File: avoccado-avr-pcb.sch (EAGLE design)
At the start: 24 parts, among them IC1 MCP1703CB, Q1 #MHz, Q2 MOSFET-NCHANNEL2N7002PW, U1 ATMEGA168#, U2 MCP73831, X1 Micro USB

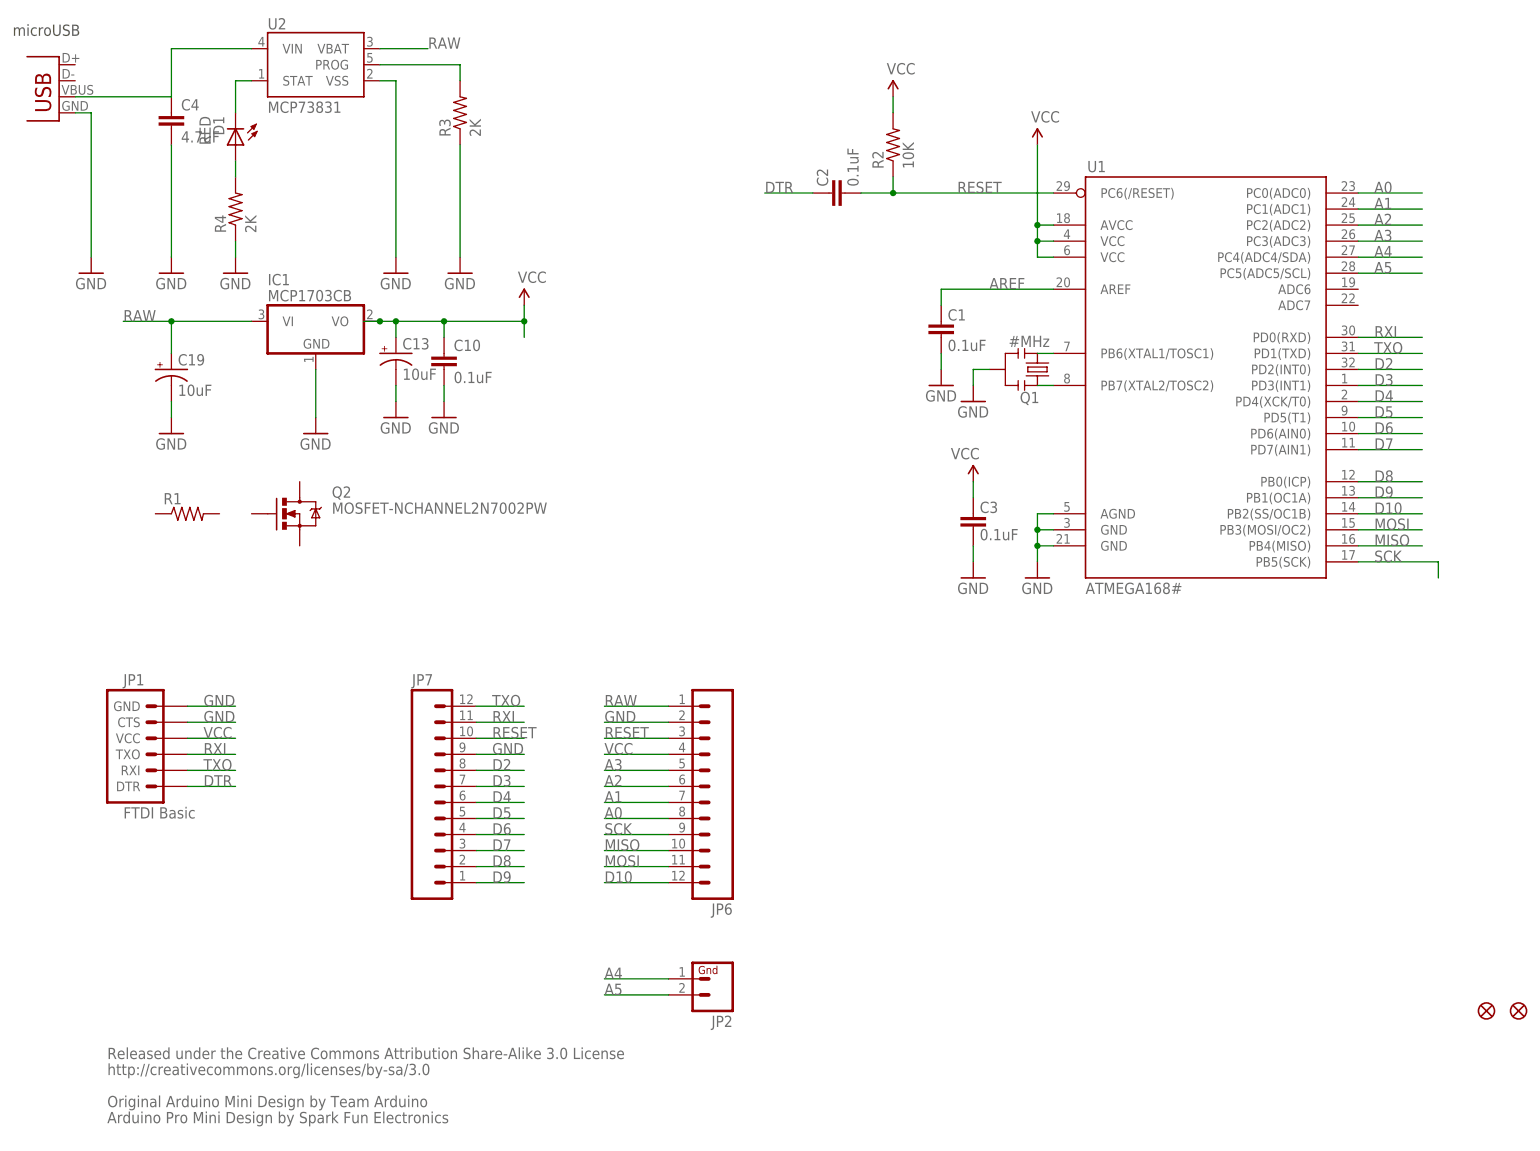
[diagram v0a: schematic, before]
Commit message: add n-chan LL mosfet for vibrator
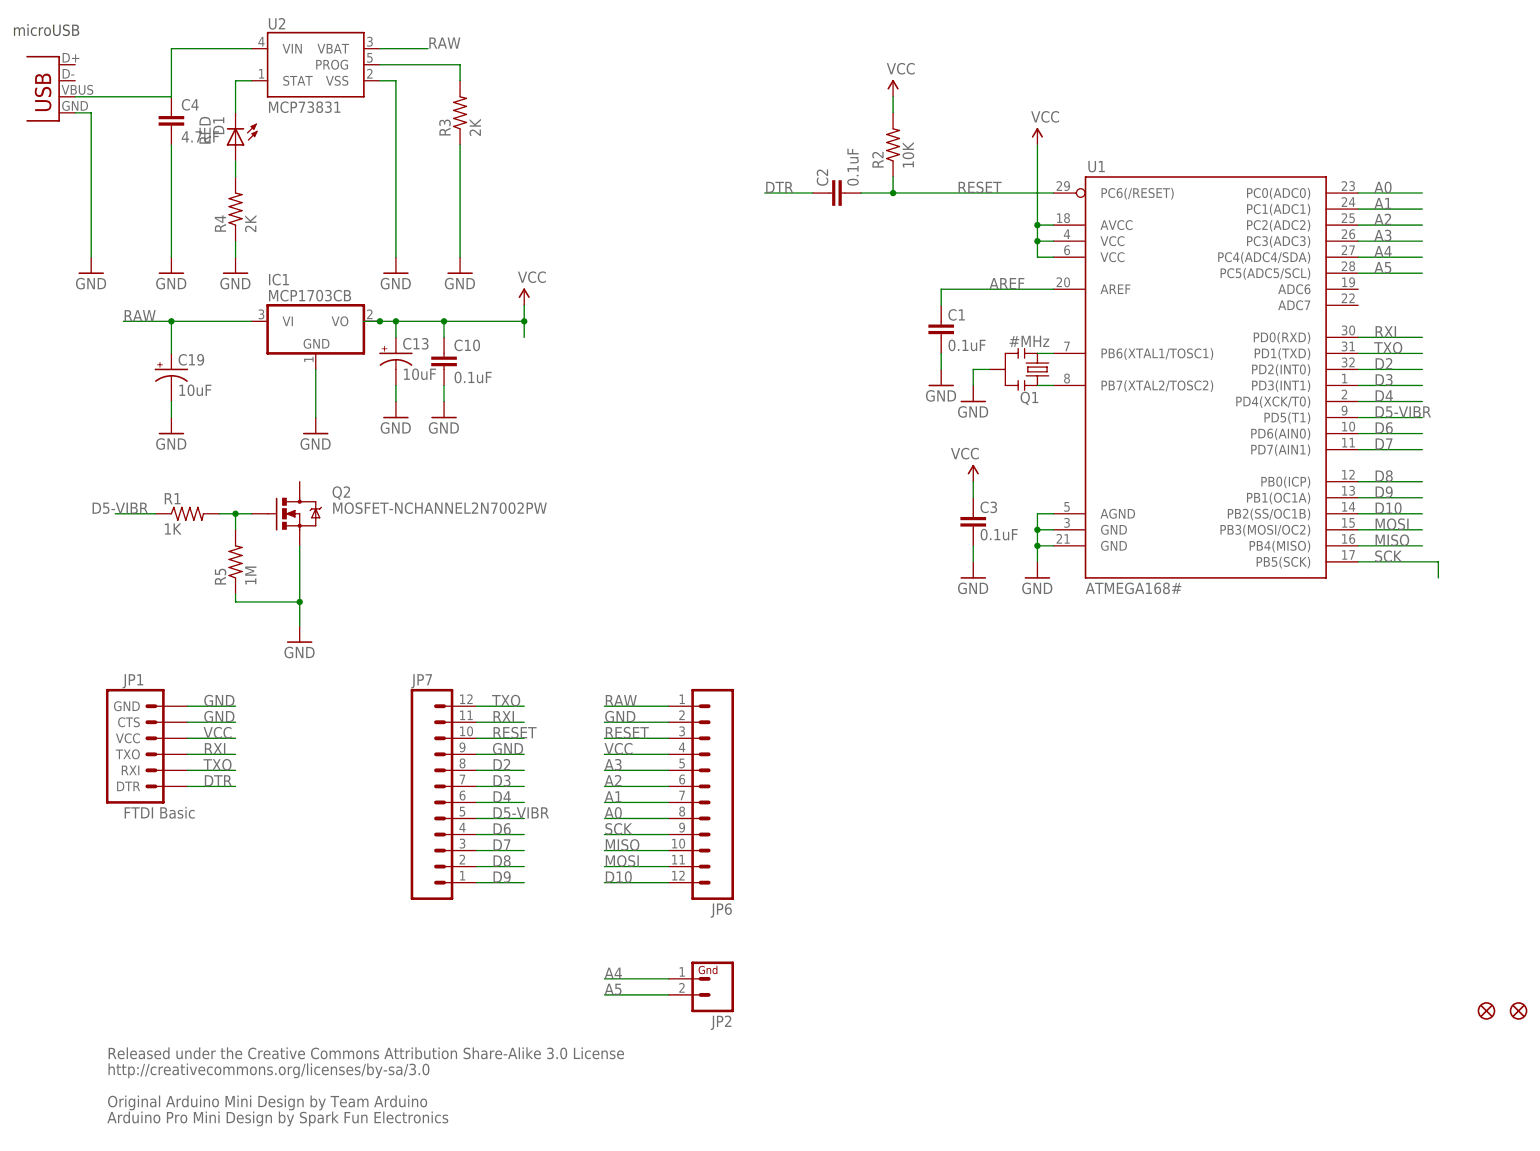
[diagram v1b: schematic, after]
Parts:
- added R5: 1M, SparkFun-Passives:RESISTOR0805-RES
- R1: value (none) -> 1K
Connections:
- removed net D5: JP7.5, U1.PD5(T1)
- new net D5-VIBR: JP7.5, R1.1, U1.PD5(T1)
- new net N$6: Q2.G, R1.2, R5.2
- net GND: now also Q2.S, R5.1
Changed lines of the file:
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@@
 <setting verticaltext="up"/>
 </settings>
-<grid distance="0.1" unitdist="inch" unit="inch" style="lines" multiple="1" display="no" altdistance="0.01" altunitdist="inch" altunit="inch"/>
+<grid distance="0.05" unitdist="inch" unit="inch" style="lines" multiple="1" display="yes" altdistance="0.005" altunitdist="inch" altunit="inch"/>
 <layers>
 <layer number="1" name="Top" color="4" fill="1" visible="no" active="no"/>
@@
 <part name="C2" library="SparkFun" deviceset="CAP" device="0402" value="0.1uF"/>
 <part name="Q2" library="SparkFun-DiscreteSemi" deviceset="MOSFET-NCHANNEL" device="2N7002PW"/>
-<part name="R1" library="SparkFun-Passives" deviceset="RESISTOR" device="0805-RES"/>
+<part name="R1" library="SparkFun-Passives" deviceset="RESISTOR" device="0805-RES" value="1K"/>
 <part name="IC1" library="linear" deviceset="MCP1703" device="CB"/>
 <part name="U2" library="SparkFun" deviceset="MCP73831" device=""/>
@@
 <part name="GND6" library="SparkFun" deviceset="GND" device=""/>
 <part name="GND8" library="SparkFun" deviceset="GND" device=""/>
+<part name="GND9" library="SparkFun" deviceset="GND" device=""/>
+<part name="R5" library="SparkFun-Passives" deviceset="RESISTOR" device="0805-RES" value="1M"/>
 </parts>
 <sheets>
@@
 <instance part="GND6" gate="1" x="38.1" y="142.24"/>
 <instance part="GND8" gate="1" x="27.94" y="142.24"/>
+<instance part="GND9" gate="1" x="48.26" y="83.82"/>
+<instance part="R5" gate="G$1" x="38.1" y="96.52" rot="R90"/>
 </instances>
 <busses>
@@
 <pinref part="GND8" gate="1" pin="GND"/>
 <wire x1="27.94" y1="162.56" x2="27.94" y2="144.78" width="0.1524" layer="91"/>
+</segment>
+<segment>
+<pinref part="GND9" gate="1" pin="GND"/>
+<pinref part="Q2" gate="G$1" pin="S"/>
+<wire x1="48.26" y1="86.36" x2="48.26" y2="90.17" width="0.1524" layer="91"/>
+<wire x1="48.26" y1="90.17" x2="48.26" y2="99.06" width="0.1524" layer="91"/>
+<wire x1="48.26" y1="90.17" x2="38.1" y2="90.17" width="0.1524" layer="91"/>
+<junction x="48.26" y="90.17"/>
+<pinref part="R5" gate="G$1" pin="1"/>
+<wire x1="38.1" y1="90.17" x2="38.1" y2="91.44" width="0.1524" layer="91"/>
 </segment>
 </net>
@@
 </segment>
 </net>
-<net name="D5" class="0">
+<net name="D5-VIBR" class="0">
 <segment>
 <wire x1="76.2" y1="55.88" x2="83.82" y2="55.88" width="0.1524" layer="91"/>
@@
 <label x="218.44" y="119.38" size="1.778" layer="95"/>
 <pinref part="U1" gate="G$1" pin="PD5(T1)"/>
+</segment>
+<segment>
+<pinref part="R1" gate="G$1" pin="1"/>
+<wire x1="25.4" y1="104.14" x2="19.05" y2="104.14" width="0.1524" layer="91"/>
+<label x="15.24" y="104.14" size="1.778" layer="95"/>
 </segment>
 </net>
@@
 </segment>
 </net>
+<net name="N$6" class="0">
+<segment>
+<pinref part="R1" gate="G$1" pin="2"/>
+<pinref part="Q2" gate="G$1" pin="G"/>
+<wire x1="35.56" y1="104.14" x2="38.1" y2="104.14" width="0.1524" layer="91"/>
+<pinref part="R5" gate="G$1" pin="2"/>
+<wire x1="38.1" y1="104.14" x2="40.64" y2="104.14" width="0.1524" layer="91"/>
+<wire x1="38.1" y1="101.6" x2="38.1" y2="104.14" width="0.1524" layer="91"/>
+<junction x="38.1" y="104.14"/>
+</segment>
+</net>

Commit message: m
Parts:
- D1: value RED -> CHARGE LED
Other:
- note added: "Original Arduino Pro Mini Design by Spark Fun Electronics"
- note added: "Released under the Creative Commons Attribution Share-Alike 4.0 License"
- note removed: "Arduino Pro Mini Design by Spark Fun Electronics"
- note removed: "Released under the Creative Commons Attribution Share-Alike 3.0 License"
- note removed: "http://creativecommons.org/licenses/by-sa/3.0"
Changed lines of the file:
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@@
 <part name="R3" library="SparkFun-Resistors" deviceset="RESISTOR" device="0805-RES" value="2K"/>
 <part name="GND3" library="SparkFun" deviceset="GND" device=""/>
-<part name="D1" library="SparkFun" deviceset="LED" device="0603" value="RED"/>
+<part name="D1" library="SparkFun" deviceset="LED" device="0603" value="CHARGE LED"/>
 <part name="GND15" library="SparkFun" deviceset="GND" device=""/>
 <part name="X1" library="SparkFun" deviceset="USB" device="-MICROB" value="Micro USB"/>
@@
 <sheet>
 <plain>
-<text x="17.78" y="17.78" size="1.778" layer="95">Released under the Creative Commons Attribution Share-Alike 3.0 License</text>
-<text x="17.78" y="15.24" size="1.778" layer="95">http://creativecommons.org/licenses/by-sa/3.0</text>
+<text x="17.78" y="17.78" size="1.778" layer="95">Released under the Creative Commons Attribution Share-Alike 4.0 License</text>
 <text x="17.78" y="10.16" size="1.778" layer="95">Original Arduino Mini Design by Team Arduino</text>
-<text x="17.78" y="7.62" size="1.778" layer="95">Arduino Pro Mini Design by Spark Fun Electronics</text>
+<text x="17.78" y="7.62" size="1.778" layer="95">Original Arduino Pro Mini Design by Spark Fun Electronics</text>
 <text x="2.794" y="179.832" size="1.778" layer="97">microUSB</text>
 </plain>

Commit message: wip change to SMD headers
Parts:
- added JP10, JP17, JP3, JP4, JP5, JP8, JP9: (no value), SparkFun-Connectors:M04SMD
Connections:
- net A0: now also JP5.1
- net A1: now also JP5.2
- net A2: now also JP5.3
- net A3: now also JP5.4
- net D10: now also JP4.1
- net D2: now also JP10.4
- net D3: now also JP10.3
- net D4: now also JP10.2
- net D5-VIBR: now also JP10.1
- net D6: now also JP17.4
- net D7: now also JP17.3
- net D8: now also JP17.2
- net D9: now also JP17.1
- net GND: now also JP8.3, JP9.1
- net MISO: now also JP4.3
- net MOSI: now also JP4.2
- net RAW: now also JP8.4
- net RESET: now also JP8.2, JP9.2
- net RXI: now also JP9.3
- net SCK: now also JP4.4
- net TXO: now also JP9.4
- net VCC: now also JP8.1
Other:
- moved on the sheet: JP6

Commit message: evaluating SMD pads
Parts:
- removed JP10, JP17, JP3, JP5, JP8, JP9: (no value), SparkFun-Connectors:M04SMD
- JP4: value (none) -> M01SMD-4.5X1.5; device SparkFun-Connectors:M04SMD -> SparkFun-Connectors:M01SMD-4.5X1.5
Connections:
- net A0: no longer JP5.1
- net A1: no longer JP5.2
- net A2: no longer JP5.3
- net A3: no longer JP5.4
- net D10: no longer JP4.1
- net D2: no longer JP10.4
- net D3: no longer JP10.3
- net D4: no longer JP10.2
- net D5-VIBR: no longer JP10.1
- net D6: no longer JP17.4
- net D7: no longer JP17.3
- net D8: no longer JP17.2
- net D9: no longer JP17.1
- net GND: no longer JP8.3, JP9.1
- net MISO: no longer JP4.3
- net MOSI: no longer JP4.2
- net RAW: no longer JP8.4
- net RESET: no longer JP8.2, JP9.2
- net RXI: no longer JP9.3
- net SCK: no longer JP4.4
- net TXO: no longer JP9.4
- net VCC: no longer JP8.1
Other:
- moved on the sheet: JP6, JP7

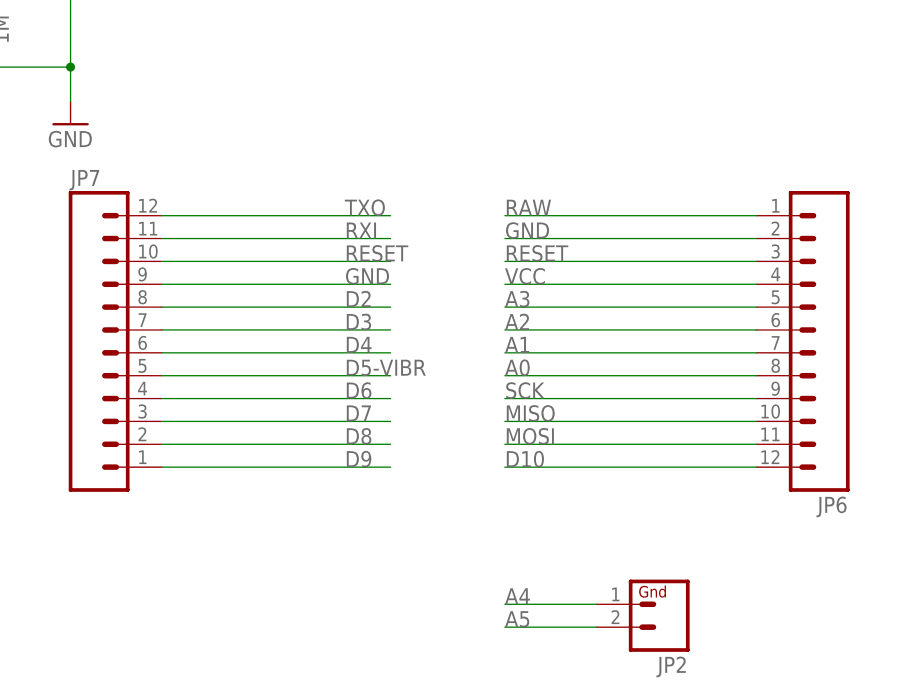
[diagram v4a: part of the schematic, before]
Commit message: exchanged THT pin rows for custom SMD pads
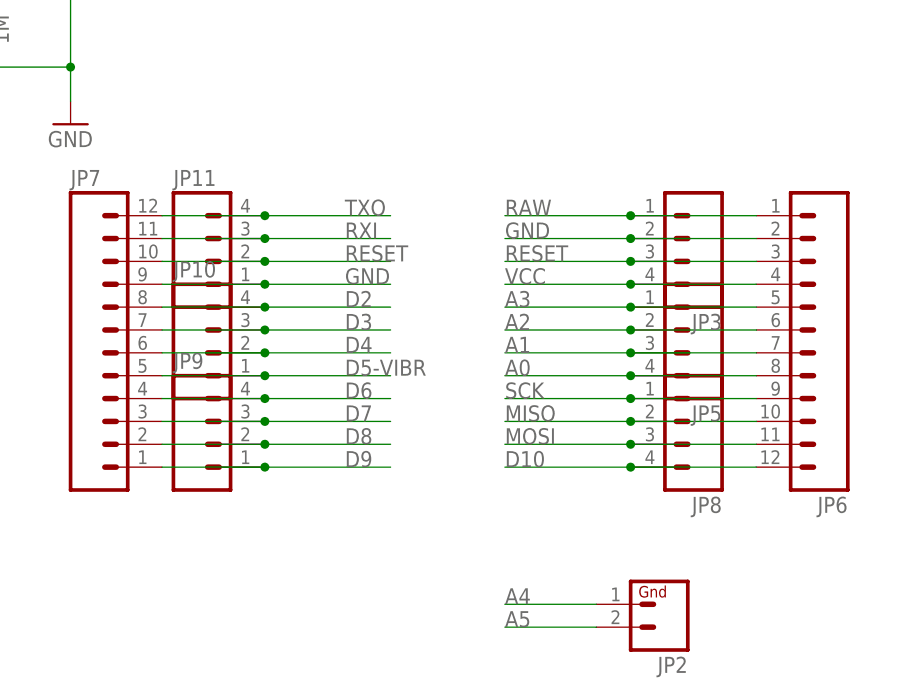
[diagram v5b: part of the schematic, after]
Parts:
- added JP10, JP11, JP3, JP5, JP8, JP9: (no value), smd-pads:M04SMD1X4
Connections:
- net A0: now also JP5.4
- net A1: now also JP5.3
- net A2: now also JP5.2
- net A3: now also JP5.1
- net D10: now also JP8.4
- net D2: now also JP10.4
- net D3: now also JP10.3
- net D4: now also JP10.2
- net D5-VIBR: now also JP10.1
- net D6: now also JP9.4
- net D7: now also JP9.3
- net D8: now also JP9.2
- net D9: now also JP9.1
- net GND: now also JP11.1, JP3.2
- net MISO: now also JP8.2
- net MOSI: now also JP8.3
- net RAW: now also JP3.1
- net RESET: now also JP11.2, JP3.3
- net RXI: now also JP11.3
- net SCK: now also JP8.1
- net TXO: now also JP11.4
- net VCC: now also JP3.4
